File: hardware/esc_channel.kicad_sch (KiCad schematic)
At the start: 39 parts, among them Q19 DOY180N03T, Q20 DOY180N03T, Q21 DOY180N03T, Q22 DOY180N03T, Q23 DOY180N03T, Q24 DOY180N03T, U10 AT32F421G8U7, U11 NSG2065Q

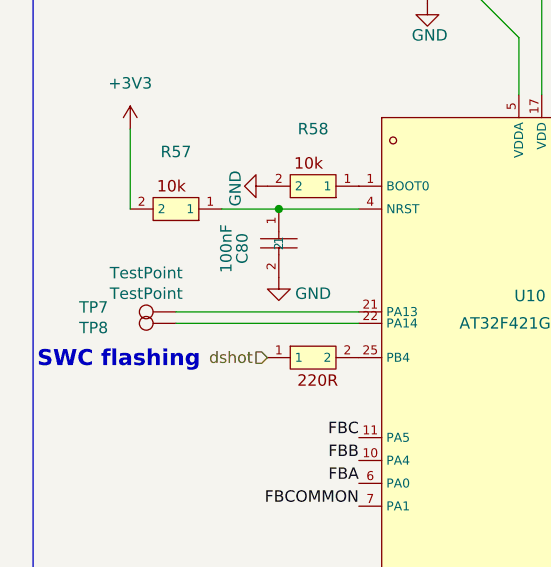
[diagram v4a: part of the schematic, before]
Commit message: Schematic readability: TP texts, C19/C107, C26, title blocks (FB5 item 6, V9-V11/M6)
- TestPoint values ('TestPoint') hidden on all sheets: the stacked TP16/TP17
  (root), TP24/TP25 and TP18/TP19/TP26/TP27 (RP2354A) texts no longer overlap.
- C19 reference/value moved left of the part (no longer printed over C107).
- C26 Description field hidden.
- Title blocks: rev r2, date 2026-10 (title added where missing) on the root,
  RP2354A, Power, IMU, OSD, Pads, ESC channel and Core interface sheets.
Edited with kicad-skip, re-saved with `kicad-cli sch upgrade --force` so the
diff stays minimal. Not done: rx_esp32c3_sx1281 and fc_blackbox title blocks
(they carry other projects' instances, OpenRX-Lite / BLACKBOX, and the headless
re-save renumbers their references); TP10 outside the frame (moving it would
detach its wire); N4 SPI0 label lift (label position is the connection point);
M7 net naming (+4v5 / +3.3V vs +3V3) left as is, it touches the LGA spec.
ERC 31 errors (unchanged).

Co-Authored-By: Claude Opus 5.5 <noreply@anthropic.com>
Claude-Session: https://claude.ai/code/session_01KTp3FLjVXfXdWrkmr6af7d
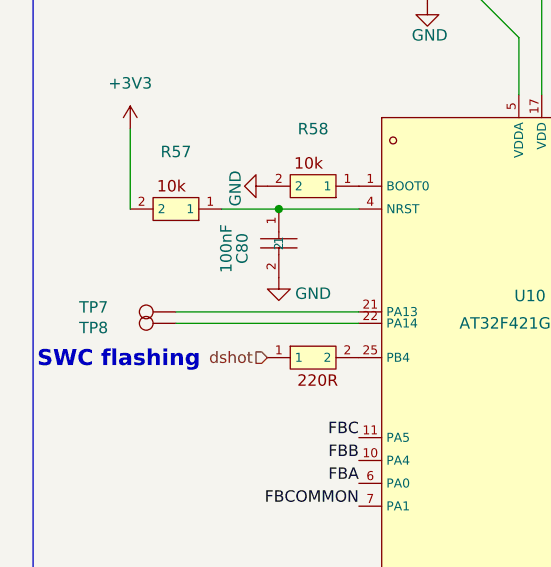
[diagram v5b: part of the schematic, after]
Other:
- title: (none) -> ESC channel
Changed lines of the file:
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@@
 	(generator_version "10.0")
 	(paper "A4")
+	(title_block
+		(title "ESC channel")
+		(date "2026-10")
+		(rev "r2")
+	)
 	(polyline
 		(pts
@@
 		(property "Value" "TestPoint"
 			(at 30.988 70.612 90)
+			(hide yes)
 			(show_name no)
 			(do_not_autoplace no)
@@
 		(property "Value" "TestPoint"
 			(at 30.988 72.898 90)
+			(hide yes)
 			(show_name no)
 			(do_not_autoplace no)

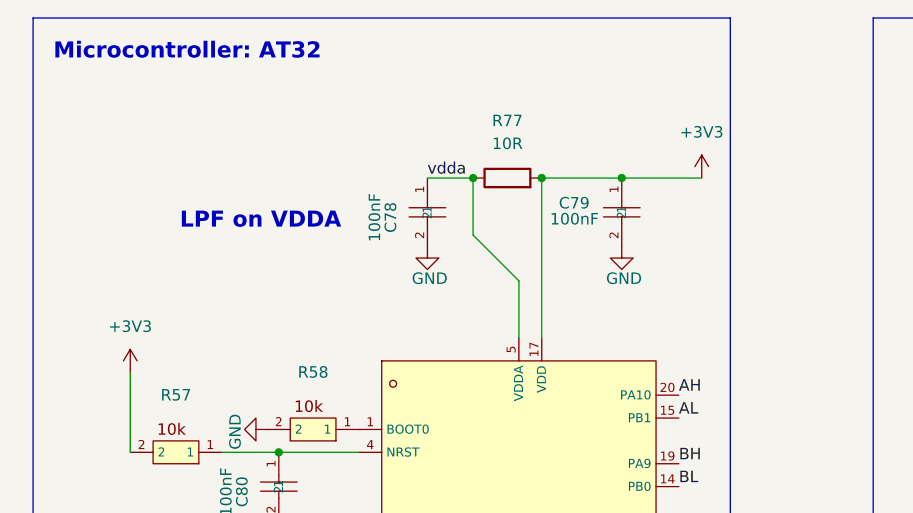
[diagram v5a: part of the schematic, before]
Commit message: ESC MCUs: battery-only +3V3_ESC from U27 TLV75533 on +5V (FB6 item 2, I3)
U27 TLV75533PDQNR (IN = EN = +5V, C110/C111 1uF 0201) makes +3V3_ESC for
U13/U15/U17/U19 VDD (pin 17) and their 16 ESC-side pins. Without a
battery the AT32s are now off, so they no longer drive the NSG2065Q
inputs while the gate-driver VCC (+10V) is 0 V. DRU: U27 mask-gang
exception (same as U23).

SD card +3V3 feed: via (69.12,69.30) -> In5 8.2 mm, inside the +10V pour
outline -> via (76.55,72.23). On In4 it cut the +BATT plane (0.596 mOhm).
+BATT measured 0.577 for In5, In2 and B.Cu and with the feed removed.
C36 restored on B (75.62,73.20).

Base identity texts are on B.Fab: there is no B.Cu GND pour spot for
0.5 mm knockout text >= 0.3 mm from pads (the only fit is under Rsense2).

Checks: Base DRC 20 (cl 15, edge 4, via_dangling 1, no new type),
parity 70; Core 27/7; ERC 31; unconnected 0/0; +BATT 0.577 mOhm (pw2
mean, 1700c87: 0.573); GND 0.356 mOhm; +5V 56.4 mV.

Co-Authored-By: Claude Opus 5.5 <noreply@anthropic.com>
Claude-Session: https://claude.ai/code/session_01KTp3FLjVXfXdWrkmr6af7d
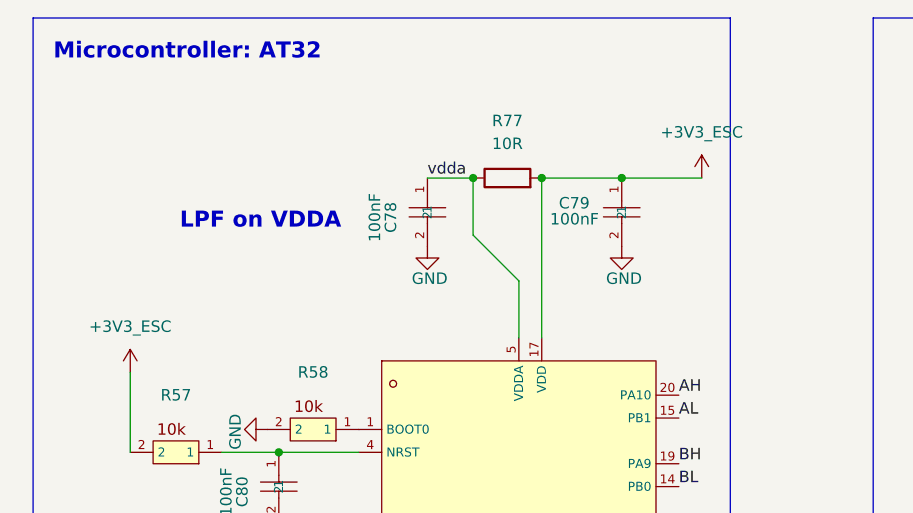
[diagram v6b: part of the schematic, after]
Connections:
- net +3V3 renamed +3V3_ESC
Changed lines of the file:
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@@
 			)
 		)
-		(property "Value" "+3V3"
+		(property "Value" "+3V3_ESC"
 			(at 29.21 49.53 0)
 			(show_name no)
@@
 			)
 		)
-		(property "Value" "+3V3"
+		(property "Value" "+3V3_ESC"
 			(at 92.71 27.94 0)
 			(show_name no)
